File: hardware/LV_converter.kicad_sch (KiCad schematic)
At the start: 35 parts, among them IC2 AP74502QTA8-7, J6 LV_THERM, Q5 IRLML0030, Q6 NVMFWS1D7N04XMT1G, Q7 NVMFWS1D7N04XMT1G, U17 TMCS1107A2UQDR, U8 V24A24C300BN3

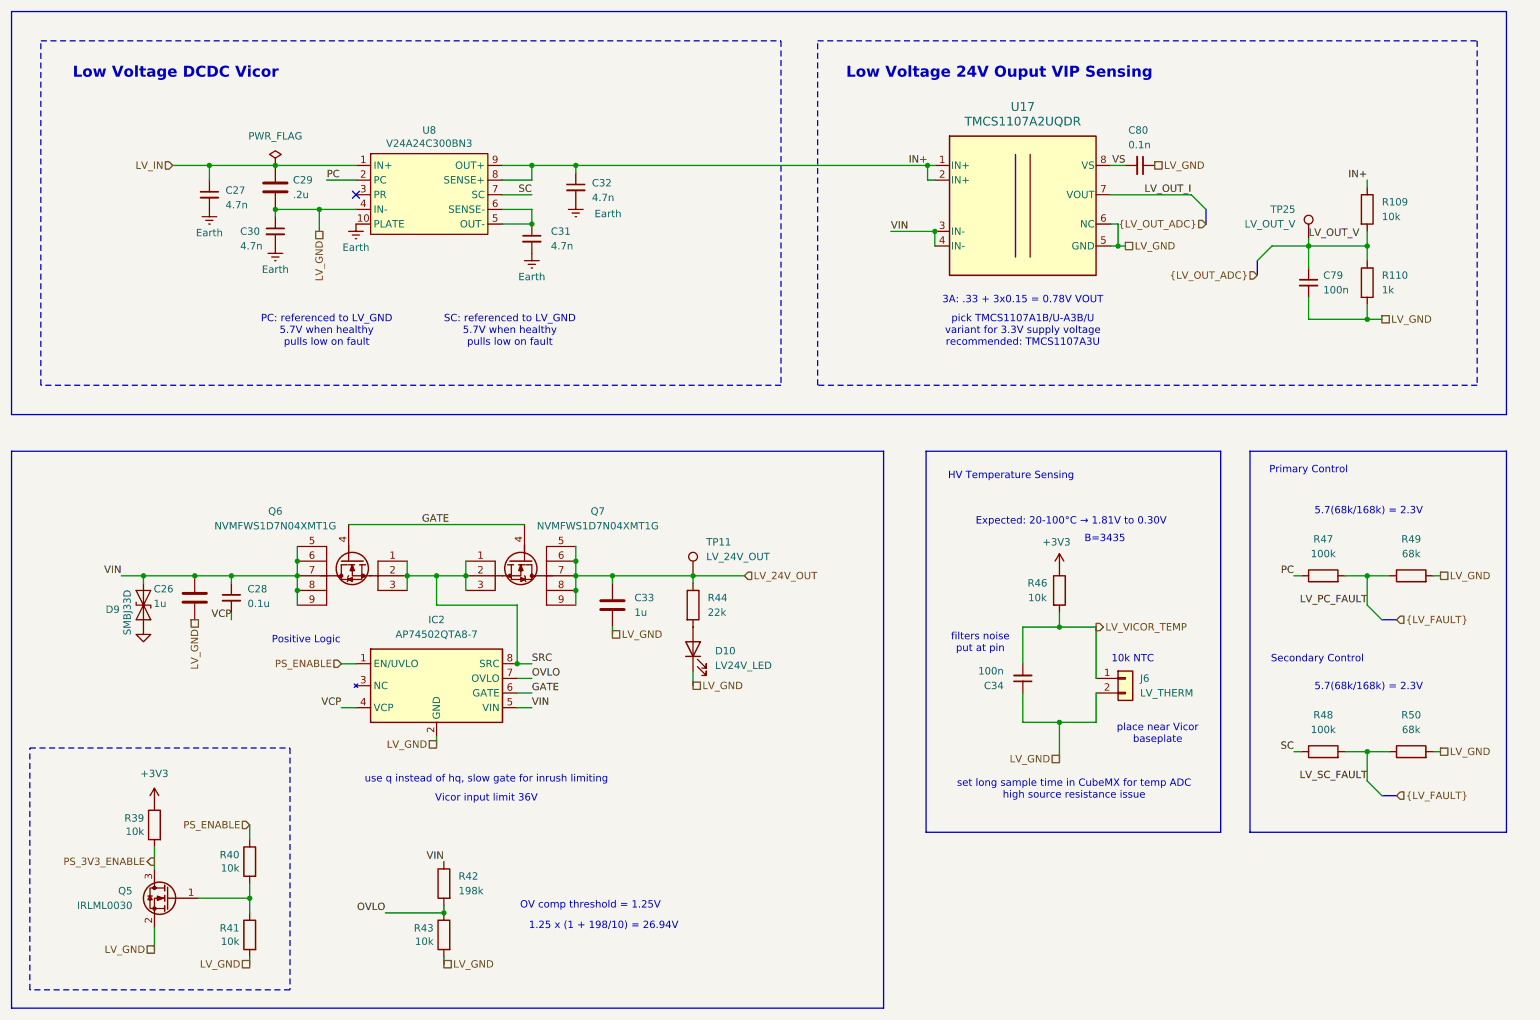
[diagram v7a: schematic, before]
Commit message: fixed up labels
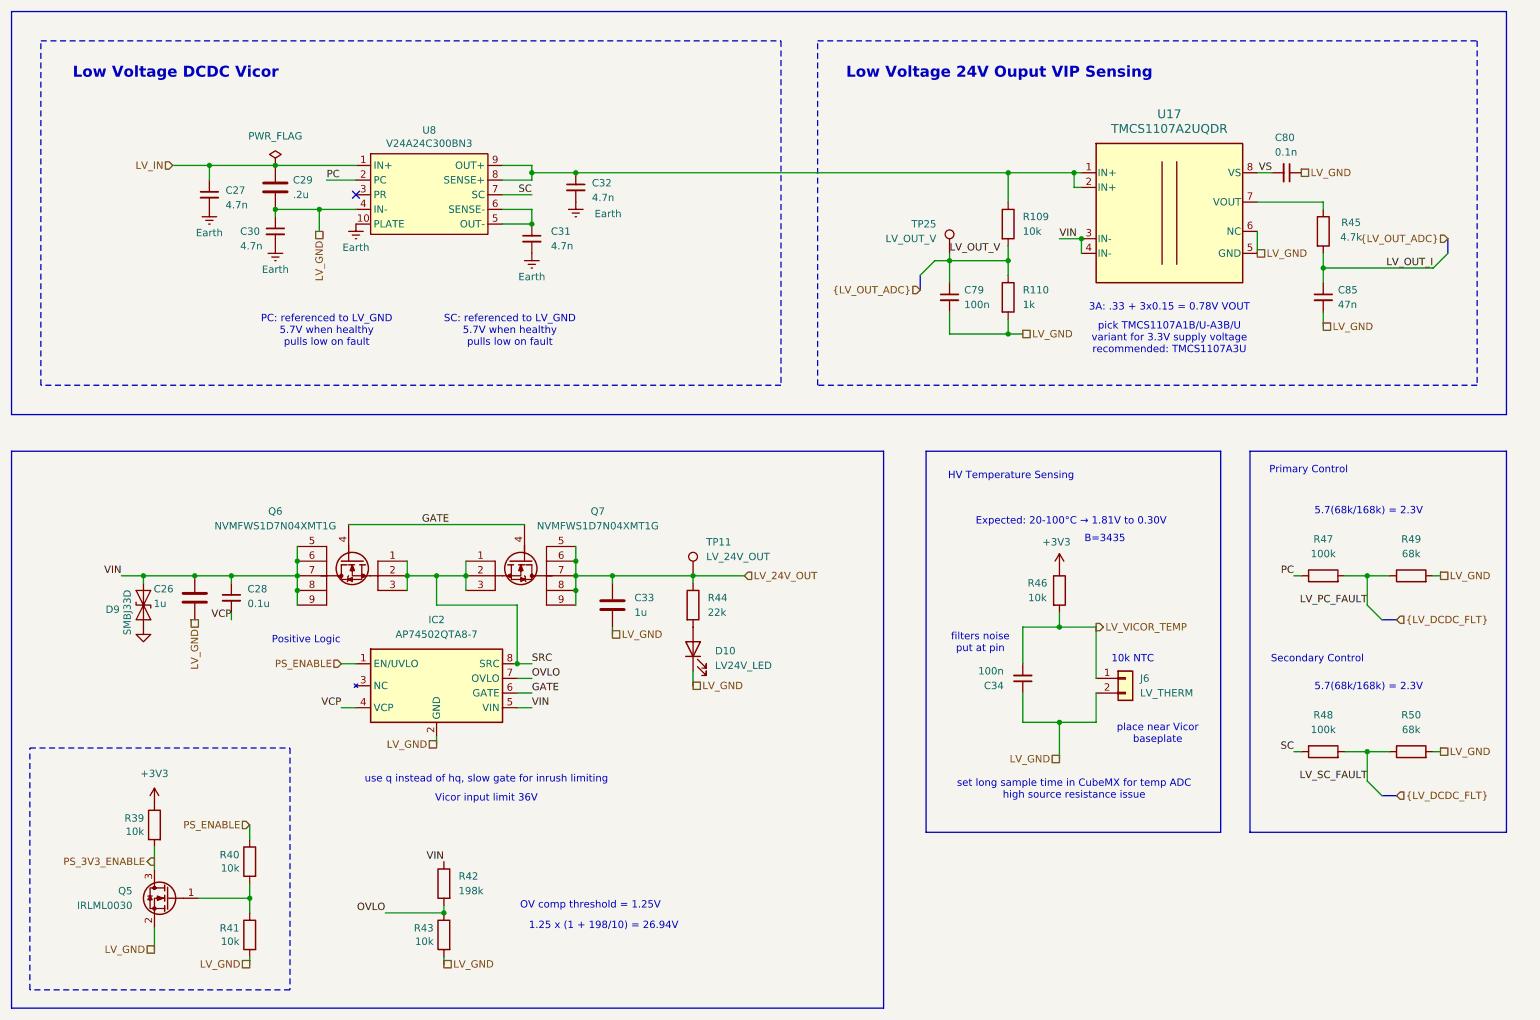
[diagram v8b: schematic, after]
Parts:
- added C85: 47n, symbol Device:C_Small
- added R45: 4.7k, Resistor_SMD:R_0603_1608Metric_Pad0.98x0.95mm_HandSolder, symbol Device:R
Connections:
- net LV_GND: now also C85.2
- net LV_OUT_I: now also C85.1, R45.2; no longer U17.7 (VOUT)
- net IN+: no longer names the net of C32.1, R109.1, U17.1 (IN+), U17.2 (IN+), U8.8 (SENSE+), U8.9 (OUT+)
- new net: R45.1, U17.7 (VOUT)
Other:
- moved on the sheet: C79, C80, R109, R110, TP25, U17
